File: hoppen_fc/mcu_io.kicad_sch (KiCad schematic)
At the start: 16 parts, among them SW1 SW_Push, SW2 SW_Push, SW3 SW_Push, U1 STM32H743ZITx, Y1 25 MHz, Y2 32.768 kHz

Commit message: work
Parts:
- C25, C26: value 20p -> 10p
- SW1, SW2, SW3: footprint (none) -> 0_misc:SW-SMD_L3.9-W3.0-P4.45; LCSC (none) -> C720477
- Y1: footprint (none) -> 0_crystals:Crystal_SMD_3225-4Pin_3.2x2.5mm; LCSC C7301943 -> C9006
- Y2: footprint (none) -> 0_crystals:Crystal_SMD_3215-2Pin
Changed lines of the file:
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@@
 		)
 	)
-	(text_box "C_S = 3p\nC_L = 12p5\nC = 2(C_L-C_S)"
+	(text_box "C_S = 7p\nC_L = 12p\nC = 2(C_L-C_S)"
 		(exclude_from_sim no)
 		(at 232.41 255.27 0)
@@
 		)
 	)
-	(text_box "C_S = 3p\nC_L = 8p\nC = 2(C_L-C_S)"
+	(text_box "C_S = 7p\nC_L = 12p\nC = 2(C_L-C_S)"
 		(exclude_from_sim no)
 		(at 184.15 255.27 0)
@@
 			)
 		)
-		(property "Footprint" ""
+		(property "Footprint" "0_crystals:Crystal_SMD_3215-2Pin"
 			(at 254 265.43 0)
 			(effects
@@
 			)
 		)
-		(property "Value" "20p"
+		(property "Value" "10p"
 			(at 267.97 270.5099 0)
 			(effects
@@
 			)
 		)
-		(property "Footprint" ""
+		(property "Footprint" "0_misc:SW-SMD_L3.9-W3.0-P4.45"
 			(at 99.06 257.81 0)
 			(effects
@@
 			)
 		)
+		(property "LCSC" "C720477"
+			(at 99.06 262.89 0)
+			(effects
+				(font
+					(size 1.27 1.27)
+				)
+				(hide yes)
+			)
+		)
 		(pin "2"
 		)
@@
 			)
 		)
-		(property "Value" "20p"
+		(property "Value" "10p"
 			(at 246.38 270.5099 0)
 			(effects
@@
 			)
 		)
-		(property "Footprint" ""
+		(property "Footprint" "0_misc:SW-SMD_L3.9-W3.0-P4.45"
 			(at 60.96 257.81 0)
 			(effects
@@
 			)
 		)
+		(property "LCSC" "C720477"
+			(at 60.96 262.89 0)
+			(effects
+				(font
+					(size 1.27 1.27)
+				)
+				(hide yes)
+			)
+		)
 		(pin "2"
 		)
@@
 			)
 		)
-		(property "Footprint" ""
+		(property "Footprint" "0_crystals:Crystal_SMD_3225-4Pin_3.2x2.5mm"
 			(at 204.47 265.43 0)
 			(effects
@@
 			)
 		)
-		(property "LCSC" "C7301943"
+		(property "LCSC" "C9006"
 			(at 204.47 265.43 0)
 			(effects
@@
 			)
 		)
-		(property "Footprint" ""
+		(property "Footprint" "0_misc:SW-SMD_L3.9-W3.0-P4.45"
 			(at 153.67 257.81 0)
 			(effects
@@
 			(at 153.67 262.89 0)
 			(effects
+				(font
+					(size 1.27 1.27)
+				)
+				(hide yes)
+			)
+		)
+		(property "LCSC" "C720477"
+			(at 153.67 262.89 0)
+			(effects

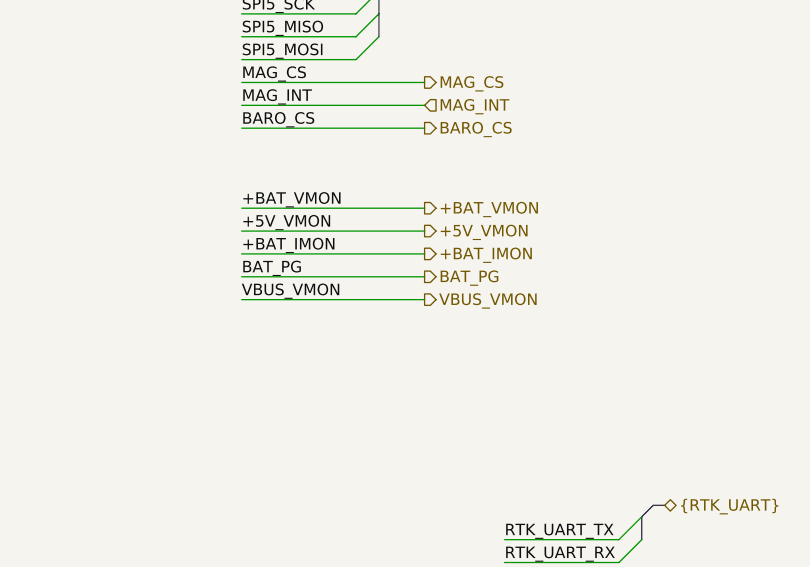
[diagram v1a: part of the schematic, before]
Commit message: power input/generation reworked
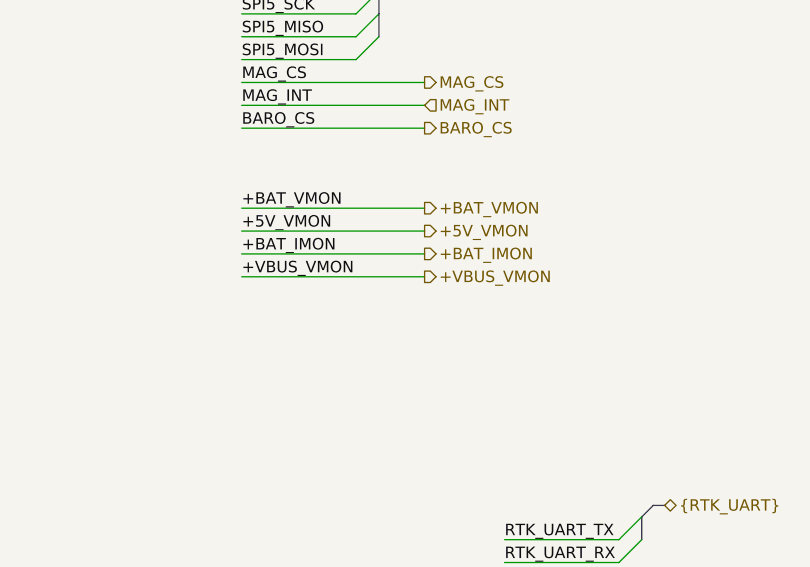
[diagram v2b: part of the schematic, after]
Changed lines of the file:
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@@
 	(wire
 		(pts
-			(xy 254 171.45) (xy 274.32 171.45)
+			(xy 254 168.91) (xy 274.32 168.91)
 		)
 		(stroke
@@
 		(pts
 			(xy 339.09 49.53) (xy 351.79 49.53)
-		)
-		(stroke
-			(width 0)
-			(type default)
-		)
-	)
-	(wire
-		(pts
-			(xy 254 168.91) (xy 274.32 168.91)
 		)
 		(stroke
@@
 		)
 	)
-	(label "VBUS_VMON"
-		(at 254 171.45 0)
+	(label "+VBUS_VMON"
+		(at 254 168.91 0)
 		(effects
 			(font
@@
 	(label "RS232_IN_TX"
 		(at 339.09 143.51 0)
-		(effects
-			(font
-				(size 1.27 1.27)
-			)
-			(justify left bottom)
-		)
-	)
-	(label "BAT_PG"
-		(at 254 168.91 0)
 		(effects
 			(font
@@
 		)
 	)
-	(hierarchical_label "BAT_PG"
-		(shape output)
-		(at 274.32 168.91 0)
-		(effects
-			(font
-				(size 1.27 1.27)
-			)
-			(justify left)
-		)
-	)
 	(hierarchical_label "INT3_GYRO"
 		(shape input)
@@
 		)
 	)
-	(hierarchical_label "VBUS_VMON"
+	(hierarchical_label "+VBUS_VMON"
 		(shape output)
-		(at 274.32 171.45 0)
-		(effects
-			(font
+		(at 274.32 168.91 0)
+		(effects
+			(font

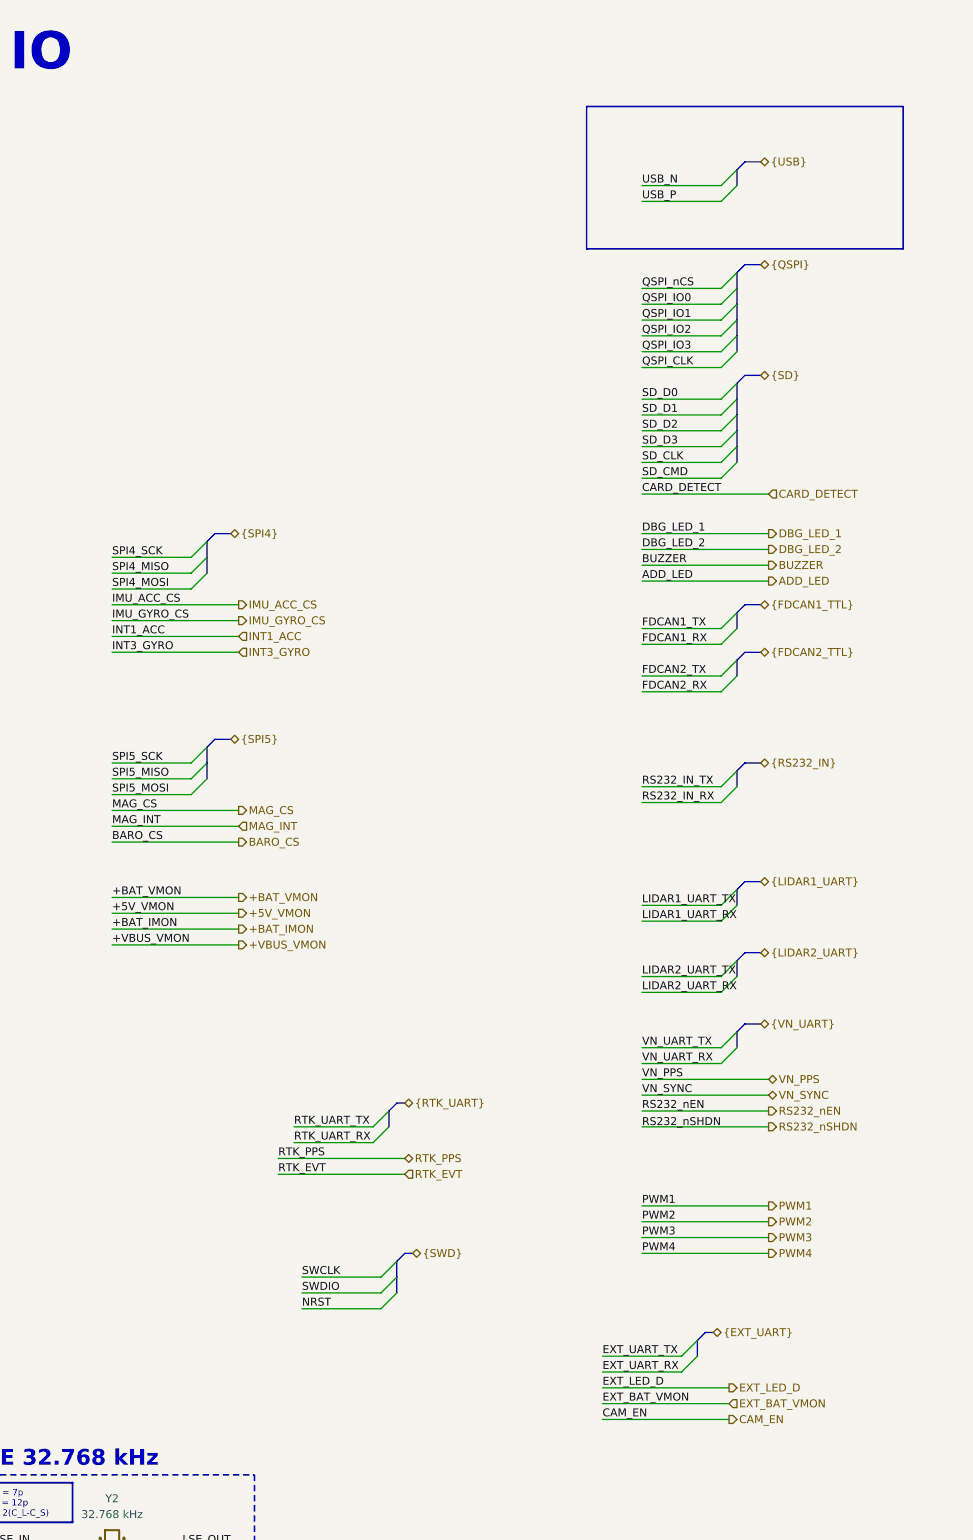
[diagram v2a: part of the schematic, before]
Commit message: finished adding lcsc numbers
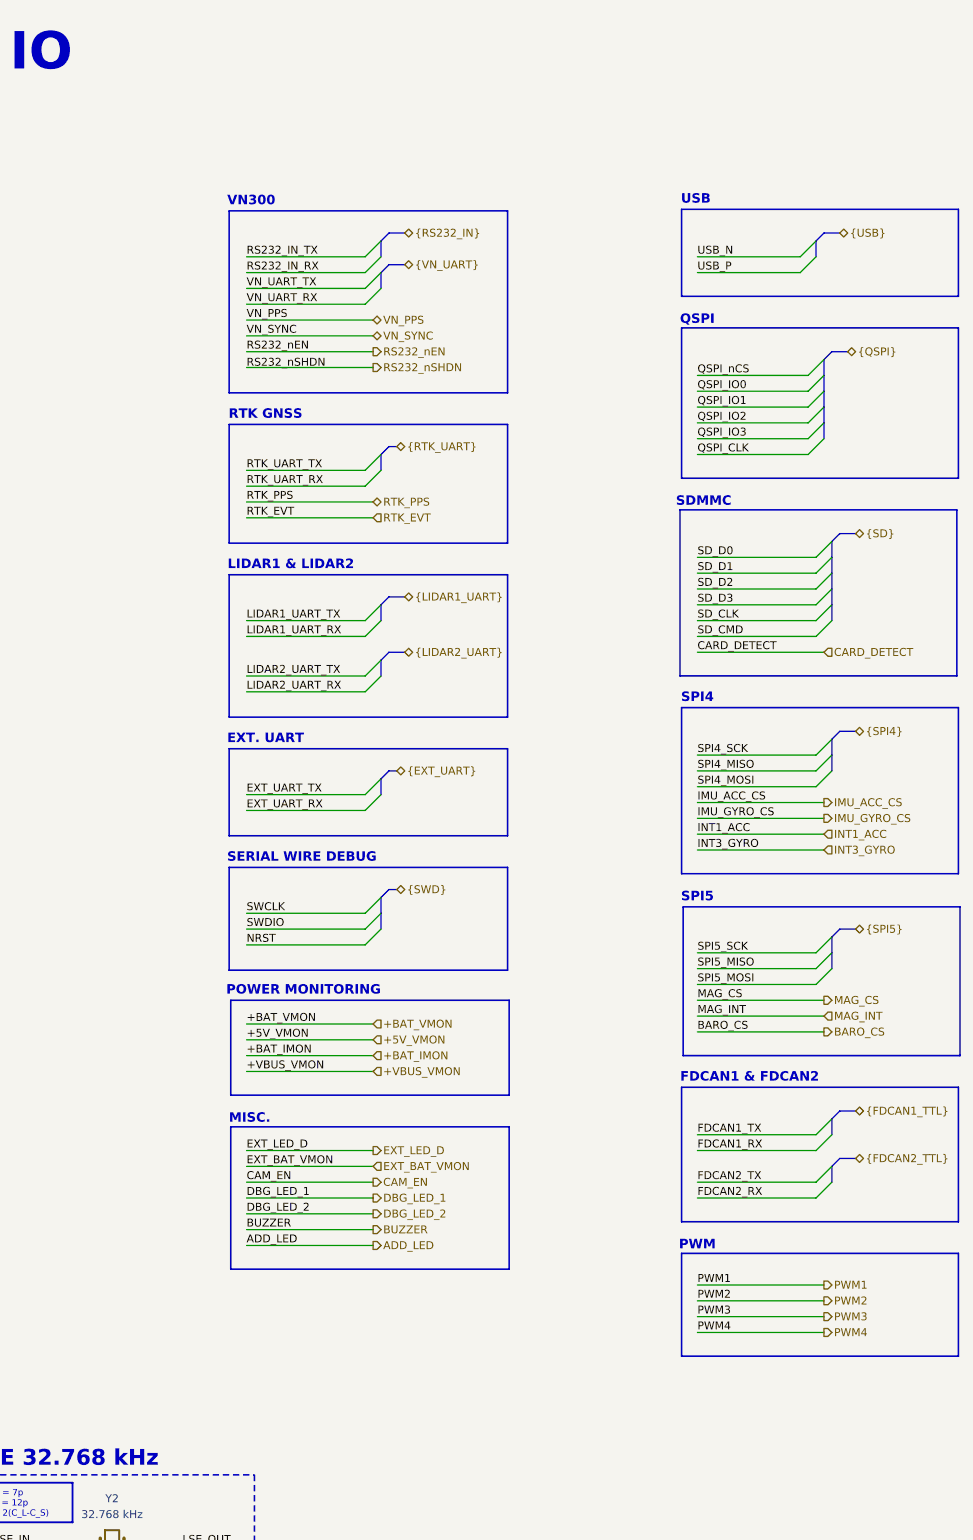
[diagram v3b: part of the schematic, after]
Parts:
- C20, C21, C22: LCSC (none) -> C307331
- C23, C24, C25, C26: LCSC (none) -> C32949
- R1: LCSC (none) -> C11702
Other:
- note added: "EXT. UART"
- note added: "FDCAN1 & FDCAN2"
- note added: "LIDAR1 & LIDAR2"
- note added: "MISC."
- note added: "POWER MONITORING"
- note added: "PWM"
- note added: "QSPI"
- note added: "RTK GNSS"
- note added: "SDMMC"
- note added: "SERIAL WIRE DEBUG"
- note added: "SPI4"
- note added: "SPI5"
- note added: "USB"
- note added: "VN300"

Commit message: ready for routing?
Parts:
- removed Y1: 25 MHz, 0_crystals:Crystal_SMD_3225-4Pin_3.2x2.5mm, symbol Device:Crystal_GND24
- added Y1: 25 MHz Crystal, 0_crystals:Crystal_SMD_3225-4Pin_3.2x2.5mm, symbol 0_crystals:25 MHz Crystal
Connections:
- net GND: now also Y1.2, Y1.4
- net HSE_IN: now also Y1.1
- net HSE_OUT: now also Y1.3

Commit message: sync
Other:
- note added: "SPI3"

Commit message: bump
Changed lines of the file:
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@@
 	(rectangle
 		(start 273.05 220.98)
-		(end 317.5 237.49)
+		(end 317.5 245.11)
 		(stroke
 			(width 0.254)
@@
 	(wire
 		(pts
-			(xy 275.59 231.14) (xy 295.91 231.14)
+			(xy 275.59 236.22) (xy 295.91 236.22)
 		)
 		(stroke
@@
 	(wire
 		(pts
+			(xy 275.59 231.14) (xy 295.91 231.14)
+		)
+		(stroke
+			(width 0)
+			(type default)
+		)
+	)
+	(wire
+		(pts
 			(xy 114.3 88.9) (xy 124.46 88.9)
 		)
@@
 	(wire
 		(pts
+			(xy 275.59 233.68) (xy 295.91 233.68)
+		)
+		(stroke
+			(width 0)
+			(type default)
+		)
+	)
+	(wire
+		(pts
 			(xy 68.58 262.89) (xy 68.58 273.05)
 		)
@@
 	(wire
 		(pts
-			(xy 275.59 233.68) (xy 295.91 233.68)
+			(xy 275.59 238.76) (xy 295.91 238.76)
 		)
 		(stroke
@@
 		)
 	)
-	(label "PWM2"
+	(label "ESC_TX_1"
 		(at 275.59 228.6 0)
 		(effects
@@
 		)
 	)
+	(label "PWM2"
+		(at 275.59 231.14 0)
+		(effects
+			(font
+				(size 1.27 1.27)
+			)
+			(justify left bottom)
+		)
+	)
 	(label "RST"
 		(at 85.09 262.89 0)
@@
 		)
 	)
+	(label "ESC_TX_2"
+		(at 275.59 233.68 0)
+		(effects
+			(font
+				(size 1.27 1.27)
+			)
+			(justify left bottom)
+		)
+	)
 	(label "QSPI_CLK"
 		(at 347.98 90.17 0)
@@
 	)
 	(label "PWM3"
-		(at 275.59 231.14 0)
+		(at 275.59 236.22 0)
 		(effects
 			(font
@@
 	)
 	(label "PWM4"
-		(at 275.59 233.68 0)
+		(at 275.59 238.76 0)
 		(effects
 			(font
@@
 		)
 	)
-	(hierarchical_label "PWM2"
-		(shape output)
+	(hierarchical_label "ESC_TX_1"
+		(shape input)
 		(at 295.91 228.6 0)
 		(effects
@@
 		)
 	)
+	(hierarchical_label "ESC_TX_2"
+		(shape input)
+		(at 295.91 233.68 0)
+		(effects
+			(font
+				(size 1.27 1.27)
+			)
+			(justify left)
+		)
+	)
 	(hierarchical_label "+BAT_VMON"
 		(shape input)
@@
 	(hierarchical_label "PWM3"
 		(shape output)
-		(at 295.91 231.14 0)
+		(at 295.91 236.22 0)
 		(effects
 			(font
@@
 		)
 	)
+	(hierarchical_label "PWM1"
+		(shape output)
+		(at 295.91 231.14 0)
+		(effects
+			(font
+				(size 1.27 1.27)
+			)
+			(justify left)
+		)
+	)
 	(hierarchical_label "ADD_LED"
 		(shape output)
@@
 	(hierarchical_label "PWM4"
 		(shape output)
-		(at 295.91 233.68 0)
+		(at 295.91 238.76 0)
 		(effects
 			(font

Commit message: bump
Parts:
- added U2: PD4E1U, 0_transistors:SOT-363_SC-70-6, symbol 0_diodes:PD4E1U
- R1: LCSC C11702 -> C106235
- renumbered C20 to C23, C21 to C24, C22 to C25, C23 to C26, C24 to C27, C25 to C28, C26 to C29
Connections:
- net RST is gone; now on net NRST: C24.1, SW2.1
- net USER_BUTTON is gone; now on net USER_BTN: C23.1, SW1.1
- net +5V_VMON: now also U1.53 (PF13)
- net +BAT_IMON: now also U1.14 (PF4)
- net +BAT_VMON: now also U1.49 (PF11)
- net ADD_LED: now also U1.135 (PB5)
- net BARO_CS: now also U1.7 (PC13)
- net BOOT: now also U2.6 (D1-)
- net BUZZER: now also U1.137 (PB7)
- net CARD_DETECT: now also U1.110 (PA15)
- net DBG_LED_1: now also U1.63 (PE10)
- net DBG_LED_2: now also U1.64 (PE11)
- net ESC_TX_1: now also U1.59 (PE8)
- net ESC_TX_2: now also U1.29 (PC3_C)
- net EXT_BAT_VMON: now also U1.13 (PF3)
- net EXT_LED_D: now also U1.34 (PA0)
- net EXT_UART_RX: now also U1.133 (PB3)
- net EXT_UART_TX: now also U1.134 (PB4)
- net FDCAN1_RX: now also U1.114 (PD0)
- net FDCAN1_TX: now also U1.115 (PD1)
- net FDCAN2_RX: now also U1.73 (PB12)
- net FDCAN2_TX: now also U1.74 (PB13)
- net GND: now also U2.2 (GND)
- net IMU_ACC_CS: now also U1.36 (PA2)
- net IMU_GYRO_CS: now also U1.40 (PA4)
- net INT1_ACC: now also U1.37 (PA3)
- net INT3_GYRO: now also U1.44 (PC4)
- net LIDAR1_UART_RX: now also U1.141 (PE0)
- net LIDAR1_UART_TX: now also U1.142 (PE1)
- net LIDAR2_UART_RX: now also U1.139 (PB8)
- net LIDAR2_UART_TX: now also U1.140 (PB9)
- net MAG_CS: now also U1.3 (PE4)
- net MAG_INT: now also U1.2 (PE3)
- net NRST: now also U2.3 (D2+)
- net PWM1: now also U1.60 (PE9)
- net PWM3: now also U1.81 (PD12)
- net PWM4: now also U1.82 (PD13)
- net QSPI_CLK: now also U1.22 (PF10)
- net QSPI_IO0: now also U1.20 (PF8)
- net QSPI_IO1: now also U1.21 (PF9)
- net QSPI_IO2: now also U1.19 (PF7)
- net QSPI_IO3: now also U1.18 (PF6)
- net QSPI_nCS: now also U1.136 (PB6)
- net RADIO_CS: now also U1.70 (PB11)
- net RADIO_DIO0: now also U1.68 (PE15)
- net RADIO_DIO1: now also U1.67 (PE14)
- net RADIO_RST: now also U1.65 (PE12)
- net RS232_IN_RX: now also U1.102 (PA10)
- net RS232_IN_TX: now also U1.101 (PA9)
- net RTK_EVT: now also U1.117 (PD3)
- net RTK_PPS: now also U1.118 (PD4)
- net RTK_UART_RX: now also U1.122 (PD6)
- net RTK_UART_TX: now also U1.119 (PD5)
- net SD_CLK: now also U1.113 (PC12)
- net SD_CMD: now also U1.116 (PD2); no longer U1.34 (PA0)
- net SD_D0: now also U1.98 (PC8)
- net SD_D1: now also U1.99 (PC9)
- net SD_D2: now also U1.111 (PC10)
- net SD_D3: now also U1.112 (PC11)
- net SPI4_MISO: now also U1.4 (PE5)
- net SPI4_MOSI: now also U1.5 (PE6)
- net SPI4_SCK: now also U1.1 (PE2)
- net SWDIO: now also U1.105 (PA13)
- net VN_PPS: now also U1.100 (PA8)
- net VN_SYNC: now also U1.93 (PG8)
- net VN_UART_RX: now also U1.97 (PC7)
- net VN_UART_TX: now also U1.96 (PC6)
- net PWM2: now reaches U1.35 (PA1)
- net SPI1_SCK: now reaches U1.41 (PA5)
- net SPI1_MISO: now reaches U1.42 (PA6)
- net SPI1_MOSI: now reaches U1.43 (PA7)
- net SPI2_SCK: now reaches U1.69 (PB10)
- net SPI2_MISO: now reaches U1.75 (PB14)
- net SPI2_MOSI: now reaches U1.76 (PB15)
- net I2C_SDA: now reaches U1.10 (PF0)
- net I2C_SCL: now reaches U1.11 (PF1)
- net USER_BTN: now reaches U1.12 (PF2)
- net USER_BTN: now also U2.1 (D1+)
- net RADIO_DIO2: now reaches U1.66 (PE13)
- net PWM5: now reaches U1.85 (PD14)
- net PWM6: now reaches U1.86 (PD15)
- no-connect marks 0 -> 34
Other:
- note added: "ESD PROTECTION"
- note added: "I2C"
- moved on the sheet: C23, C24, C25, C26, C27, C28, C29, JP1, JP2, R1, SW1, SW2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

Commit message: bump
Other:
- note added: "SPI1"
- note added: "SPI2"
- note removed: "SPI3"
- note removed: "SPI5"
